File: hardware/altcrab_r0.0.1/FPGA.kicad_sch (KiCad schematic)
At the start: 22 parts, among them J6 Conn_01x05_Male, U3A LFE5U-25F-8MG285C, U3B LFE5U-25F-8MG285C, U3C LFE5U-25F-8MG285C, U3D LFE5U-25F-8MG285C, U3E LFE5U-25F-8MG285C, U3F LFE5U-25F-8MG285C, U3G LFE5U-25F-8MG285C, U3H LFE5U-25F-8MG285C, U3I LFE5U-25F-8MG285C, U6 W25Q128JVP

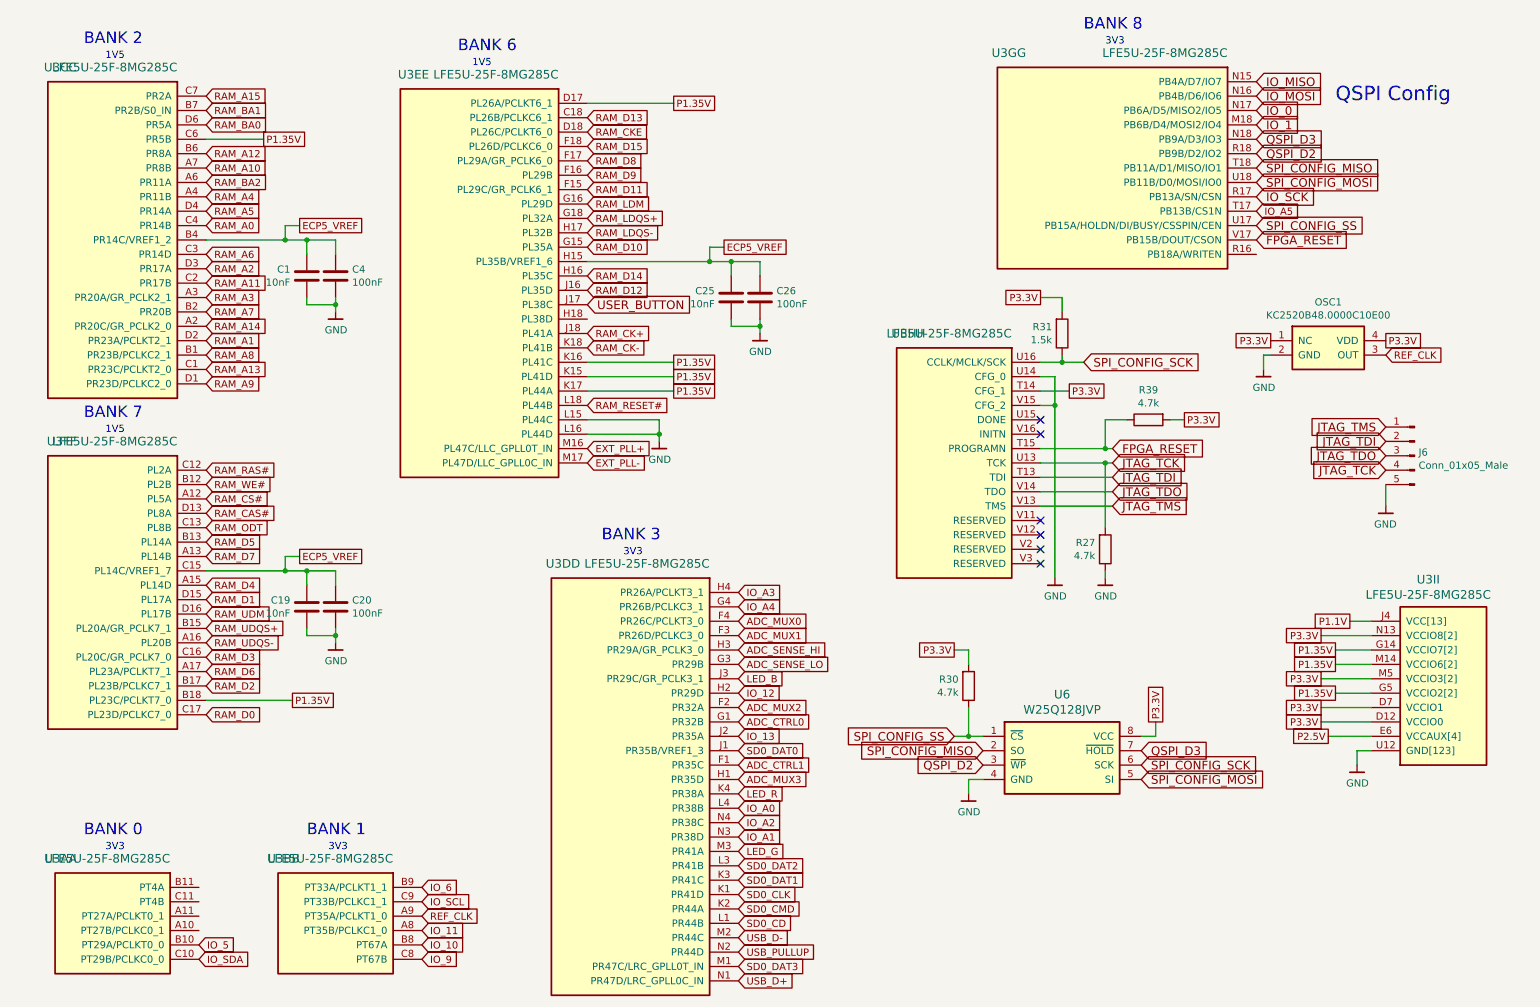
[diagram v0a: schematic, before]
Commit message: fix: KiCad 9's migration appended unit suffixes to schematic references (U3→U3A…U3I), mismatching the PCB's bare U3.
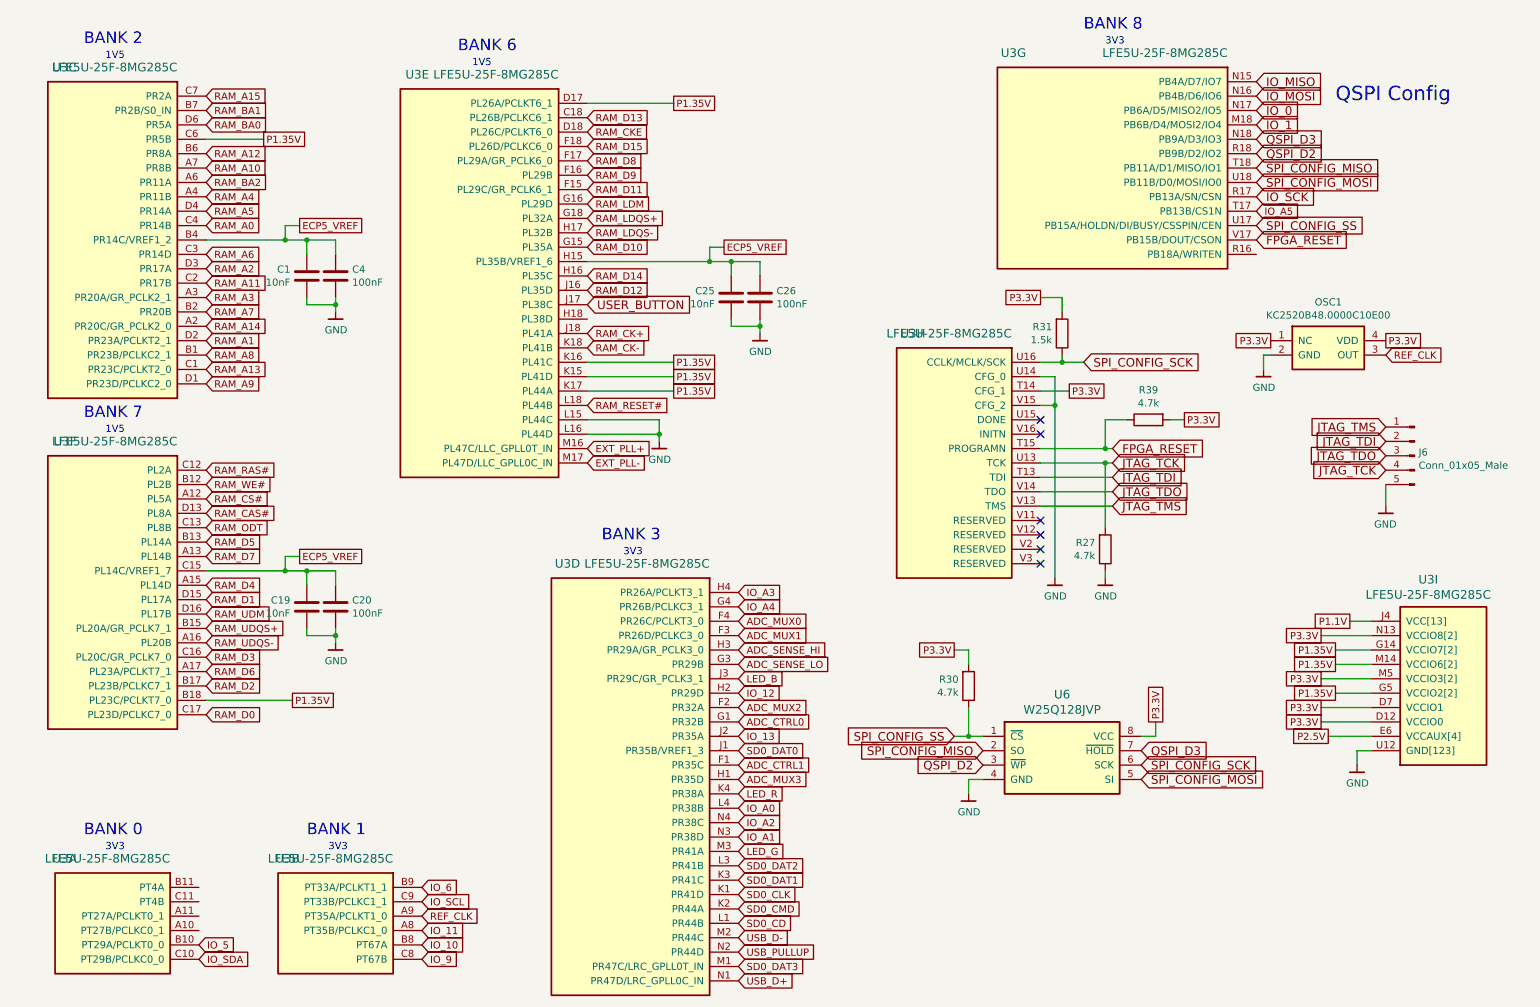
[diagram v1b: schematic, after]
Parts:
- renumbered U3A to U3, U3B to U3, U3C to U3, U3D to U3, U3E to U3, U3F to U3, U3G to U3, U3H to U3, U3I to U3
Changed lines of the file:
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@@
 		(on_board yes)
 		(dnp no)
-		(property "Reference" "U3A"
+		(property "Reference" "U3"
 			(at 27.94 166.37 0)
 			(effects
@@
 			(project "OrangeCrab"
 				(path "/098eb85a-7e69-4f62-943b-d5eb2f4a05d0/00000000-0000-0000-0000-00005ab8acb7"
-					(reference "U3A")
+					(reference "U3")
 					(unit 1)
 				)
@@
 		(on_board yes)
 		(dnp no)
-		(property "Reference" "U3B"
+		(property "Reference" "U3"
 			(at 67.31 166.37 0)
 			(effects
@@
 			(project "OrangeCrab"
 				(path "/098eb85a-7e69-4f62-943b-d5eb2f4a05d0/00000000-0000-0000-0000-00005ab8acb7"
-					(reference "U3B")
+					(reference "U3")
 					(unit 2)
 				)
@@
 		(on_board yes)
 		(dnp no)
-		(property "Reference" "U3C"
+		(property "Reference" "U3"
 			(at 27.94 26.67 0)
 			(effects
@@
 			(project "OrangeCrab"
 				(path "/098eb85a-7e69-4f62-943b-d5eb2f4a05d0/00000000-0000-0000-0000-00005ab8acb7"
-					(reference "U3C")
+					(reference "U3")
 					(unit 3)
 				)
@@
 		(on_board yes)
 		(dnp no)
-		(property "Reference" "U3D"
+		(property "Reference" "U3"
 			(at 116.84 114.3 0)
 			(effects
@@
 			(project "OrangeCrab"
 				(path "/098eb85a-7e69-4f62-943b-d5eb2f4a05d0/00000000-0000-0000-0000-00005ab8acb7"
-					(reference "U3D")
+					(reference "U3")
 					(unit 4)
 				)
@@
 		(on_board yes)
 		(dnp no)
-		(property "Reference" "U3E"
+		(property "Reference" "U3"
 			(at 90.17 27.94 0)
 			(effects
@@
 			(project "OrangeCrab"
 				(path "/098eb85a-7e69-4f62-943b-d5eb2f4a05d0/00000000-0000-0000-0000-00005ab8acb7"
-					(reference "U3E")
+					(reference "U3")
 					(unit 5)
 				)
@@
 		(on_board yes)
 		(dnp no)
-		(property "Reference" "U3F"
+		(property "Reference" "U3"
 			(at 27.94 92.71 0)
 			(effects
@@
 			(project "OrangeCrab"
 				(path "/098eb85a-7e69-4f62-943b-d5eb2f4a05d0/00000000-0000-0000-0000-00005ab8acb7"
-					(reference "U3F")
+					(reference "U3")
 					(unit 6)
 				)
@@
 		(on_board yes)
 		(dnp no)
-		(property "Reference" "U3G"
+		(property "Reference" "U3"
 			(at 195.58 24.13 0)
 			(effects
@@
 			(project "OrangeCrab"
 				(path "/098eb85a-7e69-4f62-943b-d5eb2f4a05d0/00000000-0000-0000-0000-00005ab8acb7"
-					(reference "U3G")
+					(reference "U3")
 					(unit 7)
 				)
@@
 		(on_board yes)
 		(dnp no)
-		(property "Reference" "U3H"
+		(property "Reference" "U3"
 			(at 177.8 73.66 0)
 			(effects
@@
 			(project "OrangeCrab"
 				(path "/098eb85a-7e69-4f62-943b-d5eb2f4a05d0/00000000-0000-0000-0000-00005ab8acb7"
-					(reference "U3H")
+					(reference "U3")
 					(unit 8)
 				)
@@
 		(on_board yes)
 		(dnp no)
-		(property "Reference" "U3I"
+		(property "Reference" "U3"
 			(at 266.573 117.094 0)
 			(effects
@@
 			(project "OrangeCrab"
 				(path "/098eb85a-7e69-4f62-943b-d5eb2f4a05d0/00000000-0000-0000-0000-00005ab8acb7"
-					(reference "U3I")
+					(reference "U3")
 					(unit 9)
 				)
